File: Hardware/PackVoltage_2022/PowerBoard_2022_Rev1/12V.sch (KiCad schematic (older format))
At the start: 9 parts, among them Q1 BUK7M8R5-40HX, U58 LT1910, U59 INA281

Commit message: Actuation shit
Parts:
- added C109: 0.1uF, Capacitor_SMD:C_0603_1608Metric_Pad1.05x0.95mm_HandSolder, symbol Device:C
- added C110: 10uF, Capacitor_SMD:C_0603_1608Metric_Pad1.05x0.95mm_HandSolder, symbol Device:C
- added D44: LED, LED_SMD:LED_0603_1608Metric_Pad1.05x0.95mm_HandSolder, symbol Device:LED
- added Q22: BUK7M8R5-40HX, Package_TO_SOT_SMD:LFPAK33, symbol Transistor_FET:BUK7M8R0-40EX
- added R84: 5.1k, Resistor_SMD:R_0603_1608Metric_Pad1.05x0.95mm_HandSolder, symbol Device:R
- added R85: 330, Resistor_SMD:R_0603_1608Metric_Pad1.05x0.95mm_HandSolder, symbol Device:R
- added R86: 0.0025, Resistor_SMD:R_0603_1608Metric_Pad1.05x0.95mm_HandSolder, symbol Device:R
- added U64: LT1910, Package_SO:SOIC-8_3.9x4.9mm_P1.27mm, symbol PowerBoard_2022_Rev1-rescue:LT1910-MRDT_ICs
- added U65: INA281, Package_TO_SOT_SMD:SOT-23-5, symbol PowerBoard_2022_Rev1-rescue:INA281-MRDT_ICs
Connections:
- net +5V: now also R84.2
- net 5V: now also U65.5 (V+)
- net GND: now also C109.2, C110.2, D44.1 (K), U64.1 (GND), U65.2 (GND)
- net 12VSciLog renamed 12VSciAct
- net Anderson_SciLog renamed Anderson_SciAct
- net Current_Sense_SciLog renamed Current_Sense_SciAct
- net Driver_SciLog renamed Driver_SciAct
- new net: C109.1, U64.2 (TIMER)
- new net: R84.1, U64.3 (FAULT)
- new net: Q22.4 (G), U64.5 (GATE)
- new net: Q22.1 (S), Q22.2 (S), Q22.3 (S), R85.2, R86.1, U65.3 (+)
- new net: D44.2 (A), R85.1
- new net 12VGimAct: C110.1, Q22.5 (D), U64.6 (SENSE), U64.8 (V+)
- new net Anderson_GimAct: R86.2, U65.4 (-)
- new net Current_Sense_GimAct: U65.1
- new net Driver_GimAct: U64.4 (IN)

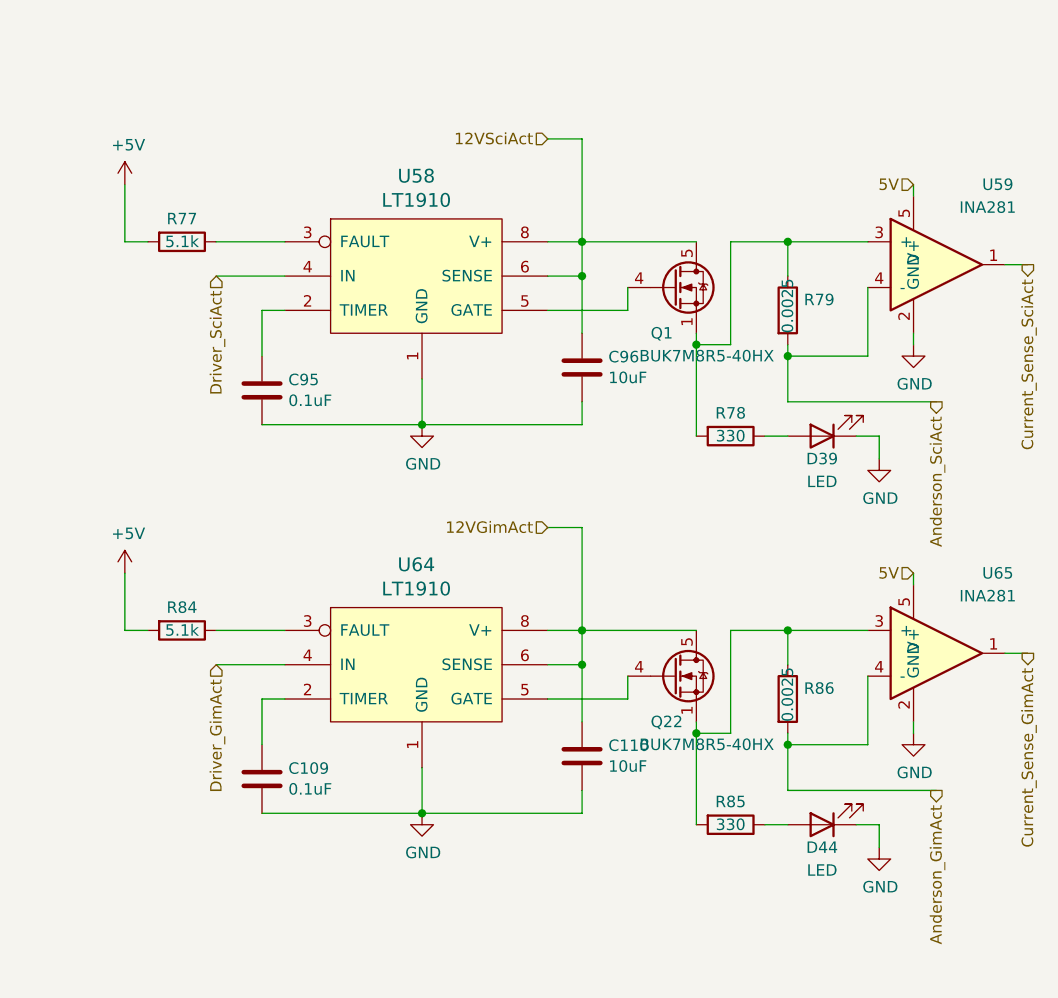
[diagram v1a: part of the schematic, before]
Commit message: Made it to layout, found out about gnd via
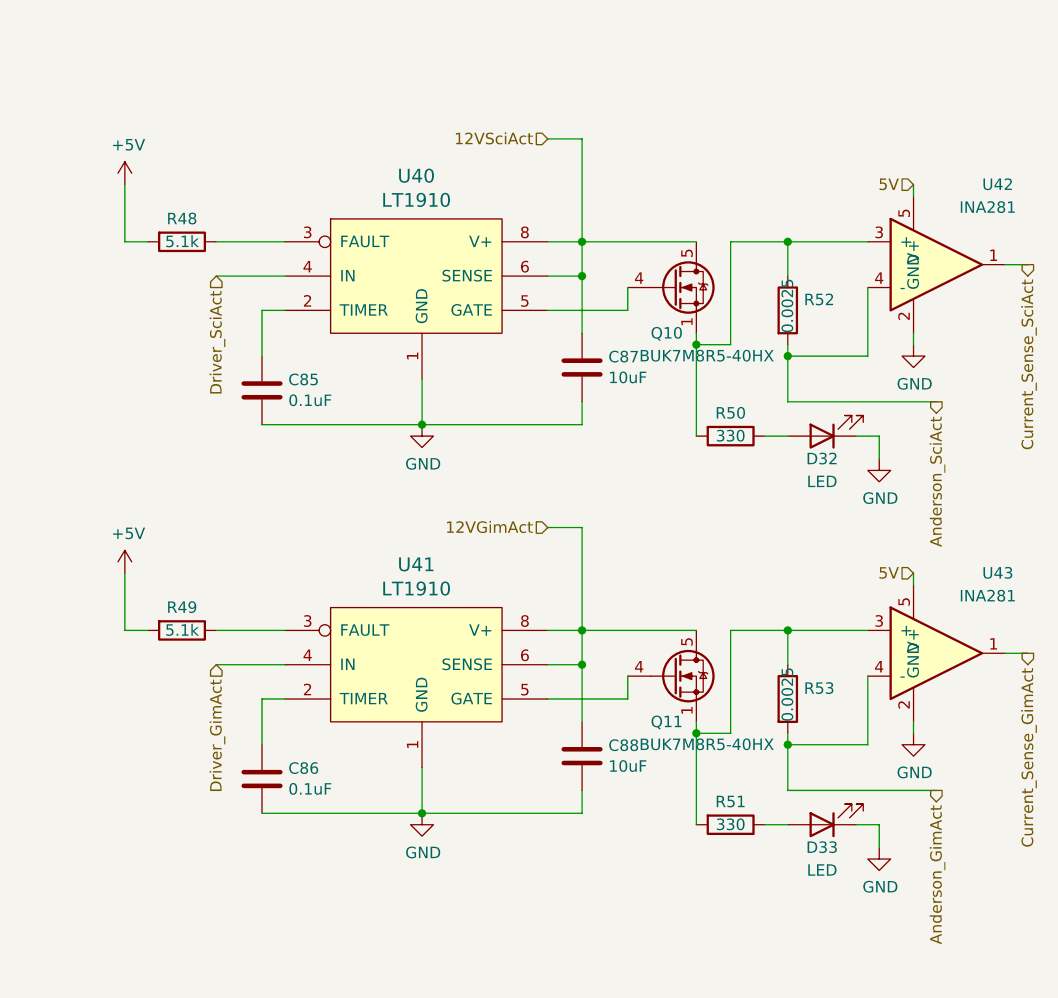
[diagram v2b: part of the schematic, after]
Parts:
- renumbered C95 to C85, C109 to C86, C96 to C87, C110 to C88, D39 to D32, D44 to D33, Q1 to Q10, Q22 to Q11, R77 to R48, R84 to R49, R78 to R50, R85 to R51, R79 to R52, R86 to R53, U58 to U40, U64 to U41, U59 to U42, U65 to U43

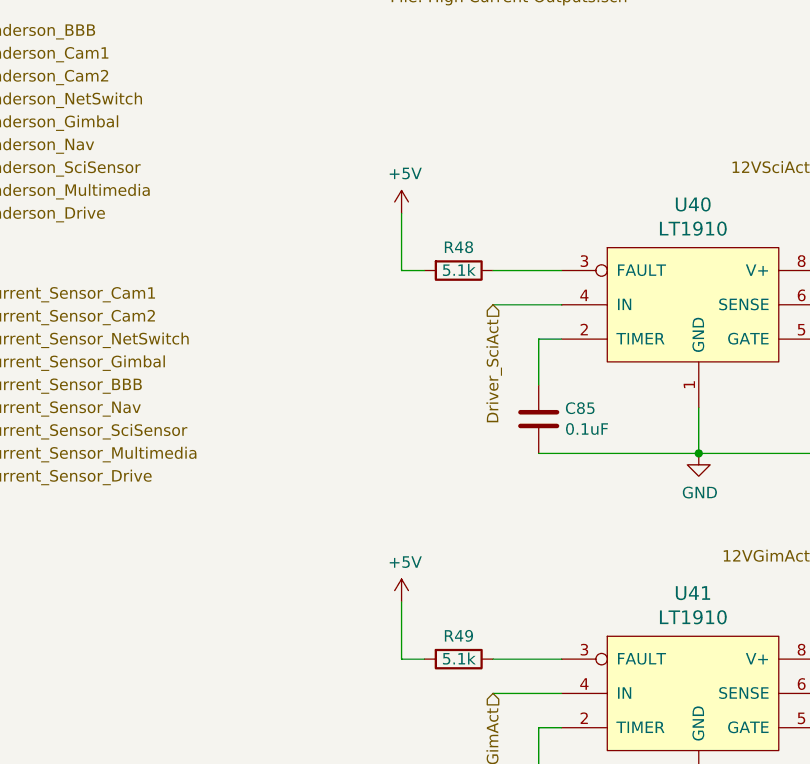
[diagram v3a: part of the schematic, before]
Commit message: Organized  Stuff into groups and changed how we organize our board
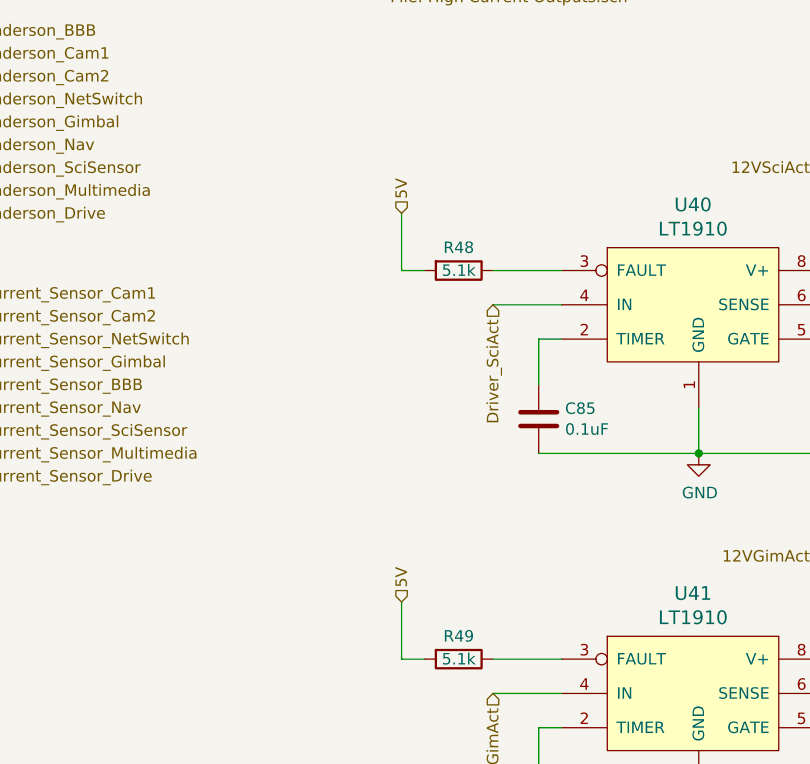
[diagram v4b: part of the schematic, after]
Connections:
- net +5V is gone; now on net 5V: R48.2, R49.2
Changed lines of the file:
@@
 EESchema Schematic File Version 4
-EELAYER 30 0
+LIBS:PowerBoard_2022_Rev1-cache
+EELAYER 26 0
 EELAYER END
 $Descr A4 11693 8268
@@
 Wire Wire Line
 	5950 3450 6250 3450
-$Comp
-L power:+5V #PWR?
-U 1 1 61F45D1B
-P 5550 3200
-AR Path="/615D5992/61F45D1B" Ref="#PWR?"  Part="1"
-AR Path="/615D7BA0/6170B60A/61F45D1B" Ref="#PWR?"  Part="1"
-AR Path="/615D7BA0/6172F88A/61F45D1B" Ref="#PWR?"  Part="1"
-AR Path="/615D7BA0/61F45D1B" Ref="#PWR0106"  Part="1"
-F 0 "#PWR0106" H 5550 3050 50  0001 C CNN
-F 1 "+5V" H 5565 3373 50  0000 C CNN
-F 2 "" H 5550 3200 50  0001 C CNN
-F 3 "" H 5550 3200 50  0001 C CNN
-	1    5550 3200
-	1    0    0    -1
-$EndComp
 Wire Wire Line
 	5550 3200 5550 3450
@@
 Wire Wire Line
 	5950 5150 6250 5150
-$Comp
-L power:+5V #PWR?
-U 1 1 61A052A9
-P 5550 4900
-AR Path="/615D5992/61A052A9" Ref="#PWR?"  Part="1"
-AR Path="/615D7BA0/6170B60A/61A052A9" Ref="#PWR?"  Part="1"
-AR Path="/615D7BA0/6172F88A/61A052A9" Ref="#PWR?"  Part="1"
-AR Path="/615D7BA0/61A052A9" Ref="#PWR0107"  Part="1"
-F 0 "#PWR0107" H 5550 4750 50  0001 C CNN
-F 1 "+5V" H 5565 5073 50  0000 C CNN
-F 2 "" H 5550 4900 50  0001 C CNN
-F 3 "" H 5550 4900 50  0001 C CNN
-	1    5550 4900
-	1    0    0    -1
-$EndComp
 Wire Wire Line
 	5550 4900 5550 5150
@@
 Wire Wire Line
 	7550 4700 7550 5150
+Text HLabel 5550 3200 1    50   Input ~ 0
+5V
+Text HLabel 5550 4900 1    50   Input ~ 0
+5V
 $EndSCHEMATC

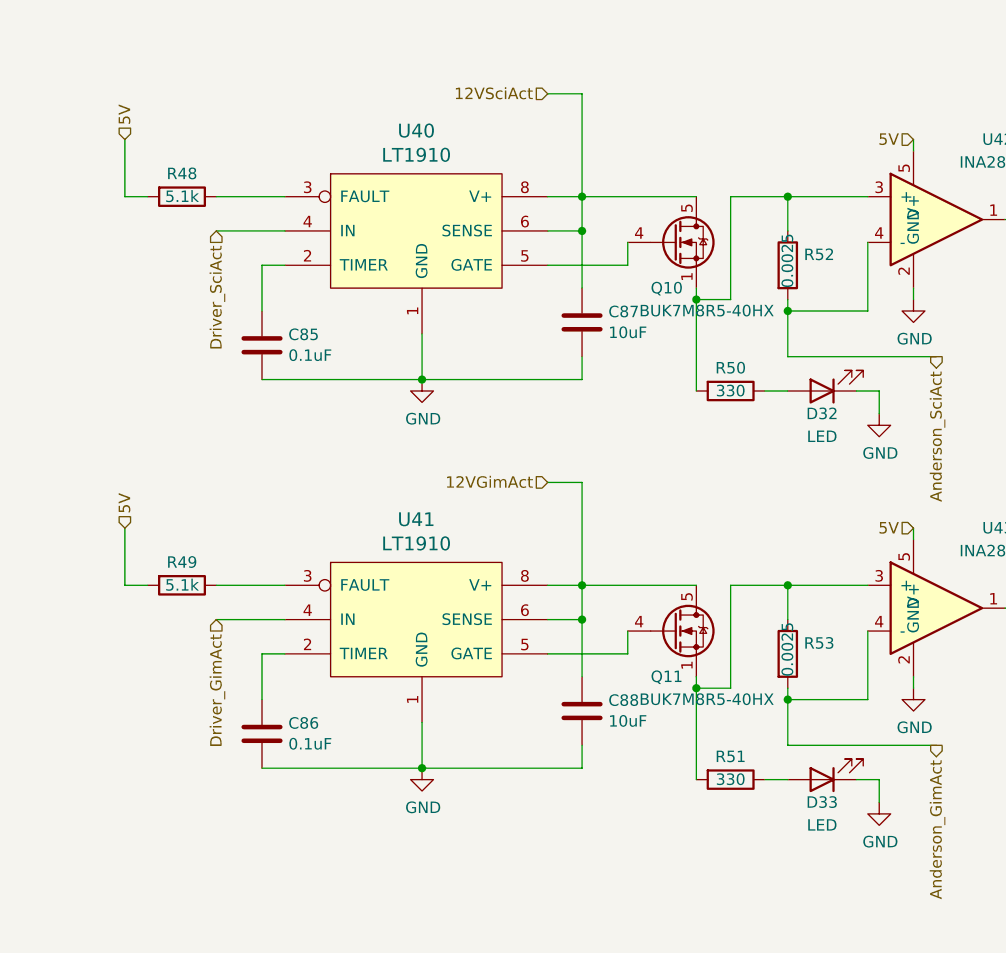
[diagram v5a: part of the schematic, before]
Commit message: Removed redundant LED's in Actuation circuits and final touches on SciAct Layout
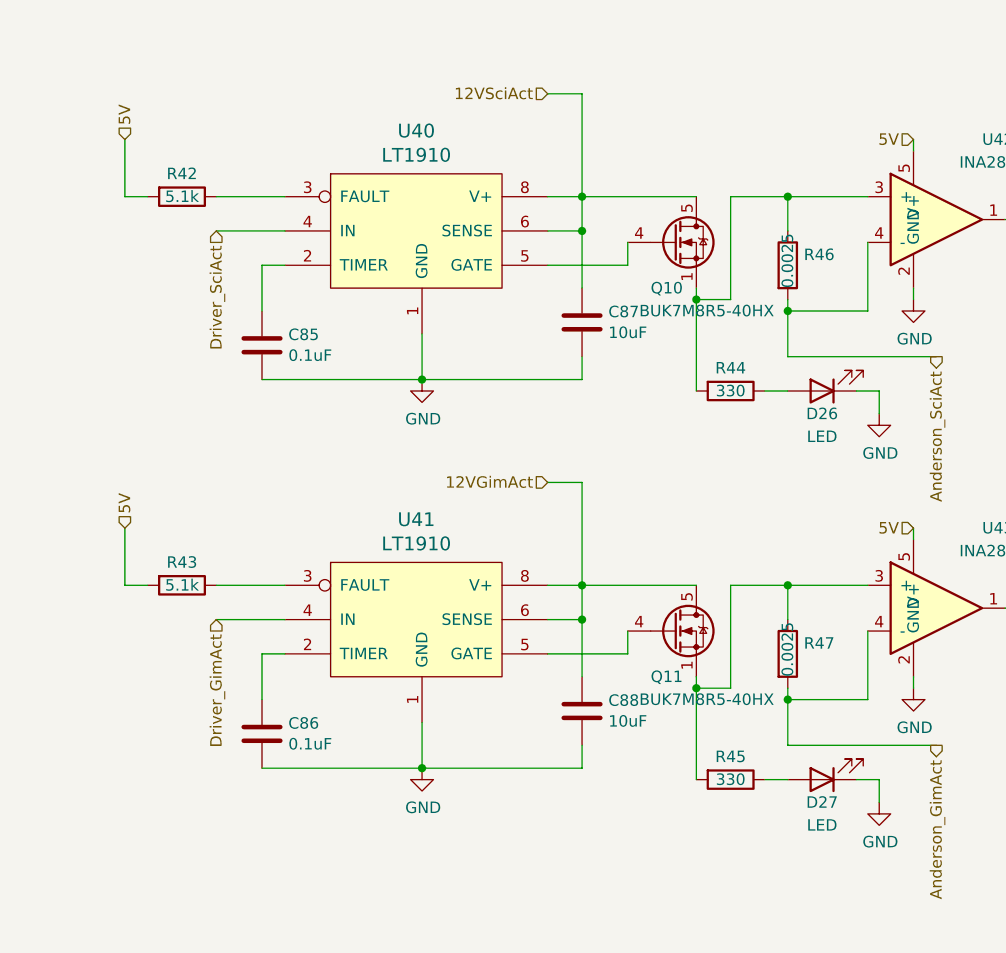
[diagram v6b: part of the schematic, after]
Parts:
- renumbered D32 to D26, D33 to D27, R48 to R42, R49 to R43, R50 to R44, R51 to R45, R52 to R46, R53 to R47
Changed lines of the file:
@@
 AR Path="/615D7BA0/6170B60A/61F45D13" Ref="R?"  Part="1"
 AR Path="/615D7BA0/6172F88A/61F45D13" Ref="R?"  Part="1"
-AR Path="/615D7BA0/61F45D13" Ref="R48"  Part="1"
-F 0 "R48" V 5700 3450 50  0000 C CNN
+AR Path="/615D7BA0/61F45D13" Ref="R42"  Part="1"
+F 0 "R42" V 5700 3450 50  0000 C CNN
 F 1 "5.1k" V 5800 3450 50  0000 C CNN
 F 2 "Resistor_SMD:R_0603_1608Metric_Pad1.05x0.95mm_HandSolder" V 5730 3450 50  0001 C CNN
@@
 AR Path="/615D7BA0/6170B60A/61F45D2C" Ref="#PWR?"  Part="1"
 AR Path="/615D7BA0/6172F88A/61F45D2C" Ref="#PWR?"  Part="1"
-AR Path="/615D7BA0/61F45D2C" Ref="#PWR0108"  Part="1"
-F 0 "#PWR0108" H 6850 4000 50  0001 C CNN
+AR Path="/615D7BA0/61F45D2C" Ref="#PWR092"  Part="1"
+F 0 "#PWR092" H 6850 4000 50  0001 C CNN
 F 1 "GND" H 6855 4077 50  0000 C CNN
 F 2 "" H 6850 4250 50  0001 C CNN
@@
 AR Path="/615D7BA0/6170B60A/61F45D47" Ref="R?"  Part="1"
 AR Path="/615D7BA0/6172F88A/61F45D47" Ref="R?"  Part="1"
-AR Path="/615D7BA0/61F45D47" Ref="R50"  Part="1"
-F 0 "R50" V 8100 4300 50  0000 C CNN
+AR Path="/615D7BA0/61F45D47" Ref="R44"  Part="1"
+F 0 "R44" V 8100 4300 50  0000 C CNN
 F 1 "330" V 8200 4300 50  0000 C CNN
 F 2 "Resistor_SMD:R_0603_1608Metric_Pad1.05x0.95mm_HandSolder" V 8130 4300 50  0001 C CNN
@@
 AR Path="/615D7BA0/6170B60A/61F45D4E" Ref="D?"  Part="1"
 AR Path="/615D7BA0/6172F88A/61F45D4E" Ref="D?"  Part="1"
-AR Path="/615D7BA0/61F45D4E" Ref="D32"  Part="1"
-F 0 "D32" H 8600 4400 50  0000 C CNN
+AR Path="/615D7BA0/61F45D4E" Ref="D26"  Part="1"
+F 0 "D26" H 8600 4400 50  0000 C CNN
 F 1 "LED" H 8600 4500 50  0000 C CNN
 F 2 "LED_SMD:LED_0603_1608Metric_Pad1.05x0.95mm_HandSolder" H 8600 4300 50  0001 C CNN
@@
 AR Path="/615D7BA0/6170B60A/61F45D55" Ref="#PWR?"  Part="1"
 AR Path="/615D7BA0/6172F88A/61F45D55" Ref="#PWR?"  Part="1"
-AR Path="/615D7BA0/61F45D55" Ref="#PWR0110"  Part="1"
-F 0 "#PWR0110" H 8850 4150 50  0001 C CNN
+AR Path="/615D7BA0/61F45D55" Ref="#PWR094"  Part="1"
+F 0 "#PWR094" H 8850 4150 50  0001 C CNN
 F 1 "GND" H 8855 4227 50  0000 C CNN
 F 2 "" H 8850 4400 50  0001 C CNN
@@
 AR Path="/615D7BA0/6170B60A/61F45D64" Ref="R?"  Part="1"
 AR Path="/615D7BA0/6172F88A/61F45D64" Ref="R?"  Part="1"
-AR Path="/615D7BA0/61F45D64" Ref="R52"  Part="1"
-F 0 "R52" H 8520 3796 50  0000 L CNN
+AR Path="/615D7BA0/61F45D64" Ref="R46"  Part="1"
+F 0 "R46" H 8520 3796 50  0000 L CNN
 F 1 "0.0025" V 8450 3650 50  0000 L CNN
 F 2 "Resistor_SMD:R_0603_1608Metric_Pad1.05x0.95mm_HandSolder" V 8380 3750 50  0001 C CNN
@@
 AR Path="/615D7BA0/6170B60A/61F45D6D" Ref="#PWR?"  Part="1"
 AR Path="/615D7BA0/6172F88A/61F45D6D" Ref="#PWR?"  Part="1"
-AR Path="/615D7BA0/61F45D6D" Ref="#PWR0112"  Part="1"
-F 0 "#PWR0112" H 9000 3650 50  0001 C CNN
+AR Path="/615D7BA0/61F45D6D" Ref="#PWR096"  Part="1"
+F 0 "#PWR096" H 9000 3650 50  0001 C CNN
 F 1 "GND" H 9005 3727 50  0000 C CNN
 F 2 "" H 9000 3900 50  0001 C CNN
@@
 AR Path="/615D7BA0/6170B60A/61A052A1" Ref="R?"  Part="1"
 AR Path="/615D7BA0/6172F88A/61A052A1" Ref="R?"  Part="1"
-AR Path="/615D7BA0/61A052A1" Ref="R49"  Part="1"
-F 0 "R49" V 5700 5150 50  0000 C CNN
+AR Path="/615D7BA0/61A052A1" Ref="R43"  Part="1"
+F 0 "R43" V 5700 5150 50  0000 C CNN
 F 1 "5.1k" V 5800 5150 50  0000 C CNN
 F 2 "Resistor_SMD:R_0603_1608Metric_Pad1.05x0.95mm_HandSolder" V 5730 5150 50  0001 C CNN
@@
 AR Path="/615D7BA0/6170B60A/61A052BA" Ref="#PWR?"  Part="1"
 AR Path="/615D7BA0/6172F88A/61A052BA" Ref="#PWR?"  Part="1"
-AR Path="/615D7BA0/61A052BA" Ref="#PWR0109"  Part="1"
-F 0 "#PWR0109" H 6850 5700 50  0001 C CNN
+AR Path="/615D7BA0/61A052BA" Ref="#PWR093"  Part="1"
+F 0 "#PWR093" H 6850 5700 50  0001 C CNN
 F 1 "GND" H 6855 5777 50  0000 C CNN
 F 2 "" H 6850 5950 50  0001 C CNN
@@
 AR Path="/615D7BA0/6170B60A/61A052D5" Ref="R?"  Part="1"
 AR Path="/615D7BA0/6172F88A/61A052D5" Ref="R?"  Part="1"
-AR Path="/615D7BA0/61A052D5" Ref="R51"  Part="1"
-F 0 "R51" V 8100 6000 50  0000 C CNN
+AR Path="/615D7BA0/61A052D5" Ref="R45"  Part="1"
+F 0 "R45" V 8100 6000 50  0000 C CNN
 F 1 "330" V 8200 6000 50  0000 C CNN
 F 2 "Resistor_SMD:R_0603_1608Metric_Pad1.05x0.95mm_HandSolder" V 8130 6000 50  0001 C CNN
@@
 AR Path="/615D7BA0/6170B60A/61A052DC" Ref="D?"  Part="1"
 AR Path="/615D7BA0/6172F88A/61A052DC" Ref="D?"  Part="1"
-AR Path="/615D7BA0/61A052DC" Ref="D33"  Part="1"
-F 0 "D33" H 8600 6100 50  0000 C CNN
+AR Path="/615D7BA0/61A052DC" Ref="D27"  Part="1"
+F 0 "D27" H 8600 6100 50  0000 C CNN
 F 1 "LED" H 8600 6200 50  0000 C CNN
 F 2 "LED_SMD:LED_0603_1608Metric_Pad1.05x0.95mm_HandSolder" H 8600 6000 50  0001 C CNN
@@
 AR Path="/615D7BA0/6170B60A/61A052E3" Ref="#PWR?"  Part="1"
 AR Path="/615D7BA0/6172F88A/61A052E3" Ref="#PWR?"  Part="1"
-AR Path="/615D7BA0/61A052E3" Ref="#PWR0111"  Part="1"
-F 0 "#PWR0111" H 8850 5850 50  0001 C CNN
+AR Path="/615D7BA0/61A052E3" Ref="#PWR095"  Part="1"
+F 0 "#PWR095" H 8850 5850 50  0001 C CNN
 F 1 "GND" H 8855 5927 50  0000 C CNN
 F 2 "" H 8850 6100 50  0001 C CNN
@@
 AR Path="/615D7BA0/6170B60A/61A052F2" Ref="R?"  Part="1"
 AR Path="/615D7BA0/6172F88A/61A052F2" Ref="R?"  Part="1"
-AR Path="/615D7BA0/61A052F2" Ref="R53"  Part="1"
-F 0 "R53" H 8520 5496 50  0000 L CNN
+AR Path="/615D7BA0/61A052F2" Ref="R47"  Part="1"
+F 0 "R47" H 8520 5496 50  0000 L CNN
 F 1 "0.0025" V 8450 5350 50  0000 L CNN
 F 2 "Resistor_SMD:R_0603_1608Metric_Pad1.05x0.95mm_HandSolder" V 8380 5450 50  0001 C CNN
@@
 AR Path="/615D7BA0/6170B60A/61A052FB" Ref="#PWR?"  Part="1"
 AR Path="/615D7BA0/6172F88A/61A052FB" Ref="#PWR?"  Part="1"
-AR Path="/615D7BA0/61A052FB" Ref="#PWR0113"  Part="1"
-F 0 "#PWR0113" H 9000 5350 50  0001 C CNN
+AR Path="/615D7BA0/61A052FB" Ref="#PWR097"  Part="1"
+F 0 "#PWR097" H 9000 5350 50  0001 C CNN
 F 1 "GND" H 9005 5427 50  0000 C CNN
 F 2 "" H 9000 5600 50  0001 C CNN

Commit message: Replaced 12v okis w/big buck. Changed .0025 resistors to not 603.
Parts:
- R46, R47: footprint Resistor_SMD:R_0603_1608Metric_Pad1.05x0.95mm_HandSolder -> Resistor_SMD:R_1206_3216Metric_Pad1.30x1.75mm_HandSolder
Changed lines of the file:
@@
 EESchema Schematic File Version 4
-LIBS:PowerBoard_2022_Rev1-cache
-EELAYER 26 0
+EELAYER 30 0
 EELAYER END
 $Descr A4 11693 8268
@@
 F 0 "R46" H 8520 3796 50  0000 L CNN
 F 1 "0.0025" V 8450 3650 50  0000 L CNN
-F 2 "Resistor_SMD:R_0603_1608Metric_Pad1.05x0.95mm_HandSolder" V 8380 3750 50  0001 C CNN
+F 2 "Resistor_SMD:R_1206_3216Metric_Pad1.30x1.75mm_HandSolder" V 8380 3750 50  0001 C CNN
 F 3 "~" H 8450 3750 50  0001 C CNN
 	1    8450 3750
@@
 F 0 "R47" H 8520 5496 50  0000 L CNN
 F 1 "0.0025" V 8450 5350 50  0000 L CNN
-F 2 "Resistor_SMD:R_0603_1608Metric_Pad1.05x0.95mm_HandSolder" V 8380 5450 50  0001 C CNN
+F 2 "Resistor_SMD:R_1206_3216Metric_Pad1.30x1.75mm_HandSolder" V 8380 5450 50  0001 C CNN
 F 3 "~" H 8450 5450 50  0001 C CNN
 	1    8450 5450
